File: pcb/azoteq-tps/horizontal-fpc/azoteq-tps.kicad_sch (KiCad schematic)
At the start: 4 parts, among them J2 Conn_01x06_Socket

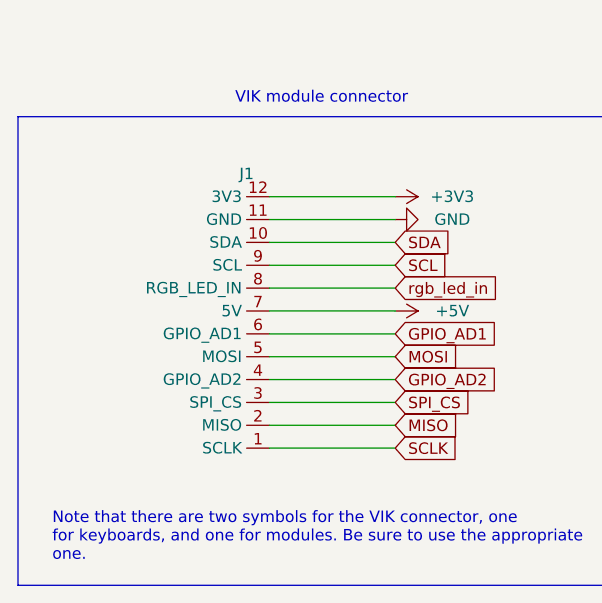
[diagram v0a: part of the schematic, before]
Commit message: updated vikm connector symbols, per some recommendations from sigprof in fingerpunch discord
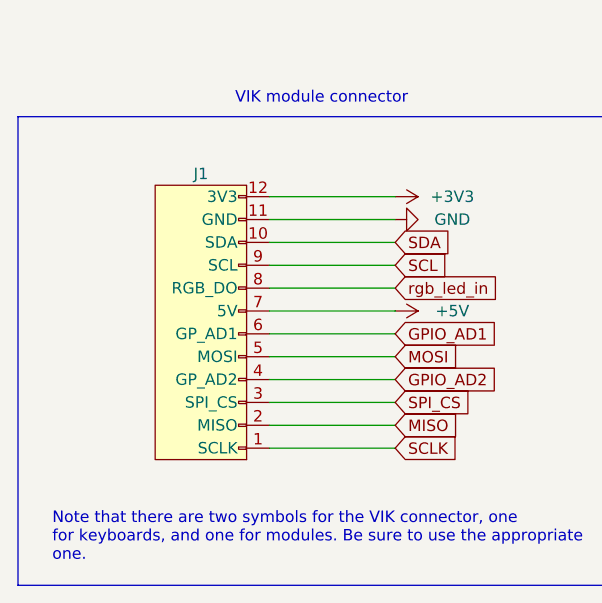
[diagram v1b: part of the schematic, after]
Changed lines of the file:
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@@
     )
   )
-  (symbol (lib_id "vik:vik-module-connector") (at 81.28 72.39 180) (unit 1)
-    (in_bom yes) (on_board yes) (dnp no) (fields_autoplaced)
-    (property "Reference" "J1" (at 78.74 55.88 0)
+  (symbol (lib_id "vik:vik-module-connector") (at 73.66 73.66 180) (unit 1)
+    (in_bom yes) (on_board yes) (dnp no)
+    (property "Reference" "J1" (at 73.66 55.88 0)
       (effects (font (size 1.27 1.27)))
     )
-    (property "Value" "~" (at 81.28 78.74 0)
+    (property "Value" "~" (at 73.66 80.01 0)
       (effects (font (size 1.27 1.27)))
     )
-    (property "Footprint" "vik:vik-module-connector-horizontal-mini" (at 81.28 78.74 0)
+    (property "Footprint" "vik:vik-module-connector-horizontal-mini" (at 73.66 80.01 0)
       (effects (font (size 1.27 1.27)) hide)
     )
-    (property "Datasheet" "https://datasheet.lcsc.com/lcsc/2111151830_HDGC-0-5K-QX-12PWB_C2919479.pdf" (at 81.28 78.74 0)
+    (property "Datasheet" "https://datasheet.lcsc.com/lcsc/2111151830_HDGC-0-5K-QX-12PWB_C2919479.pdf" (at 73.66 80.01 0)
       (effects (font (size 1.27 1.27)) hide)
     )
-    (property "LCSC" "C2919479" (at 81.28 72.39 0)
+    (property "LCSC" "C2919479" (at 73.66 73.66 0)
       (effects (font (size 1.27 1.27)) hide)
     )
